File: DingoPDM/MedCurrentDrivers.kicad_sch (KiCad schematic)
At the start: 8 parts, among them U21 LM324, U7 LM324

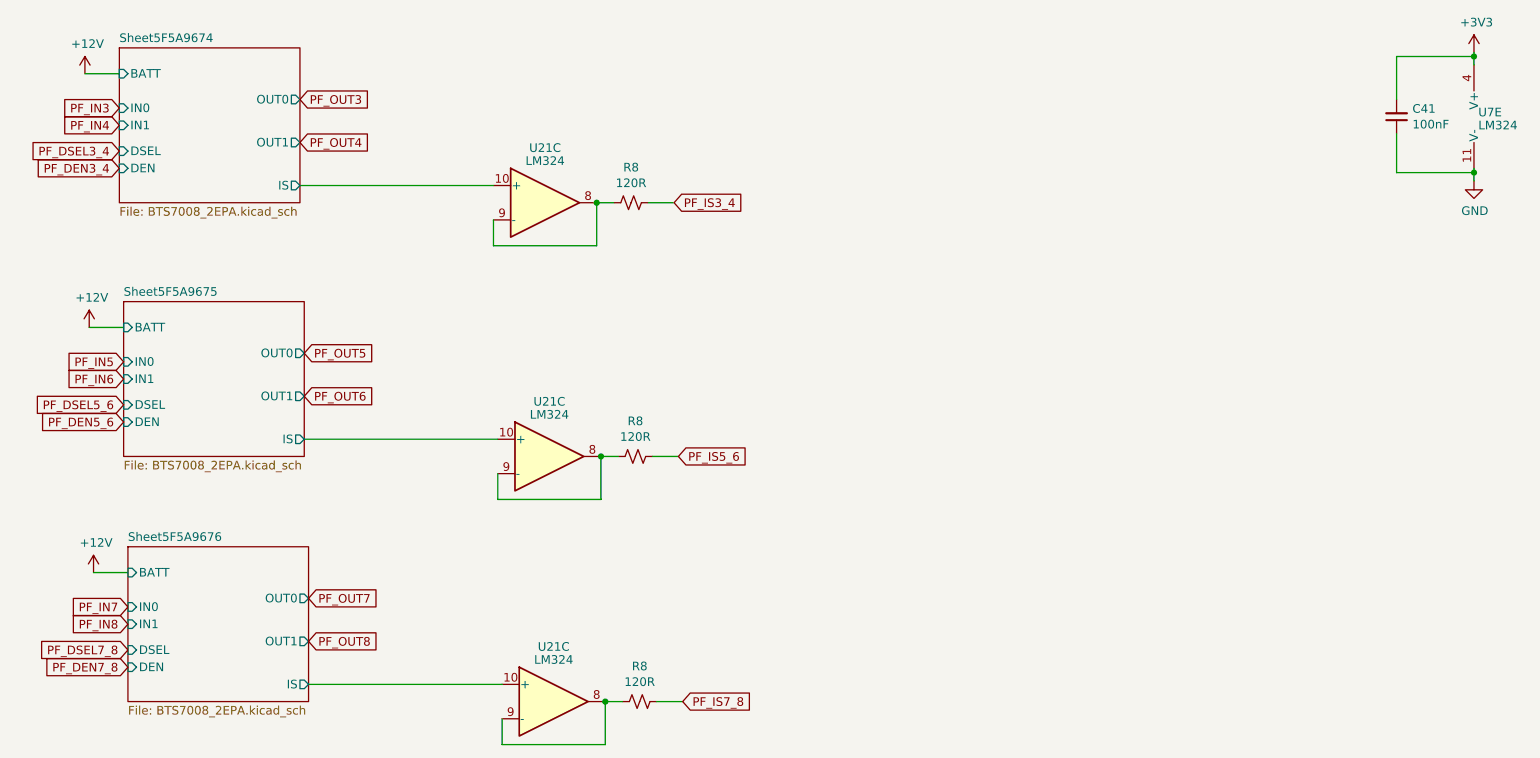
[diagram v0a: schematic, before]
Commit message: Updated to Kicad 8
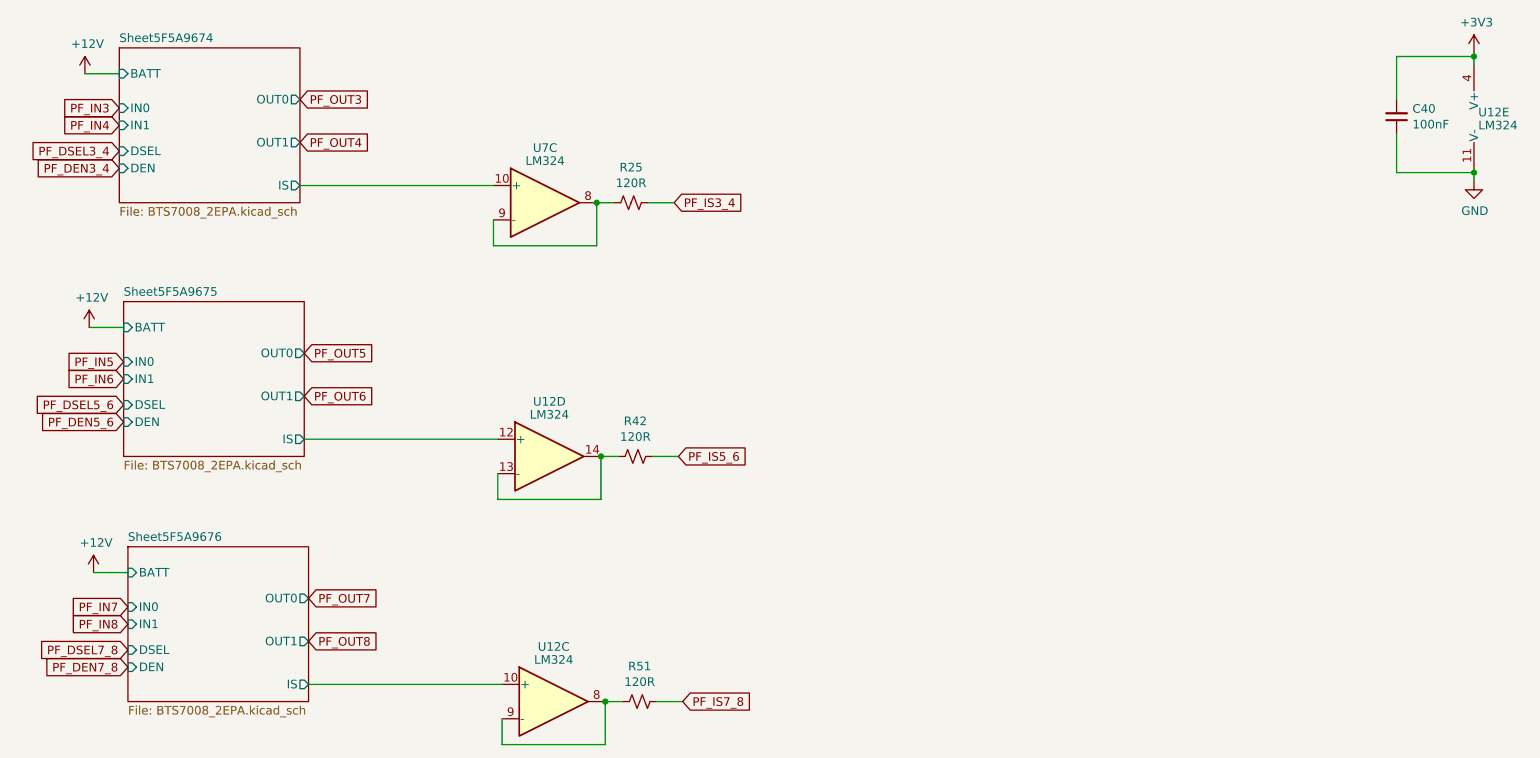
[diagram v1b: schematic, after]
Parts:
- renumbered C41 to C40, R8 to R25, R8 to R42, R8 to R51, U7 to U12, U21 to U12, U21 to U7
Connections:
- net Sheet5F5A9675/IS: now also U12.12 (+); no longer U12.10 (+)
- new net: R42.2, U12.13 (-), U12.14

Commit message: add DC-DC converter options
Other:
- title: Dingo_PDM -> dingoPDM
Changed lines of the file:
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@@
 (kicad_sch
-	(version 20231120)
+	(version 20250114)
 	(generator "eeschema")
-	(generator_version "8.0")
+	(generator_version "9.0")
 	(paper "USLetter")
 	(title_block
-		(title "Dingo_PDM")
-		(date "2024-05-26")
-		(rev "v7.3")
+		(title "dingoPDM")
+		(date "2025-05-06")
+		(rev "v7.5")
 		(comment 3 "github.com/corygrant")
 		(comment 4 "Cory Grant")
@@
 		(at 45.72 24.765)
 		(size 26.67 22.86)
+		(exclude_from_sim no)
+		(in_bom yes)
+		(on_board yes)
+		(dnp no)
 		(fields_autoplaced yes)
 		(stroke
@@
 		(at 46.99 98.425)
 		(size 26.67 22.86)
+		(exclude_from_sim no)
+		(in_bom yes)
+		(on_board yes)
+		(dnp no)
 		(fields_autoplaced yes)
 		(stroke
@@
 		(at 46.355 62.23)
 		(size 26.67 22.86)
-		(fields_autoplaced yes)
-		(stroke
+		(exclude_from_sim no)
+		(in_bom yes)
+		(on_board yes)
+		(dnp no)
+		(fields_autoplaced yes)
+		(stroke
